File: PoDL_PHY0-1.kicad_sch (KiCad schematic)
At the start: 45 parts, among them Q1 DMG3414U, Q10 DMG3414U, Q11 DMG3414U, Q12 MMBT3904, Q2 MMBTA06, Q3 MMBT3904, Q4 DMG3414U, Q5 DMG3414U, Q6 MMBT3904, Q7 DMG3414U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

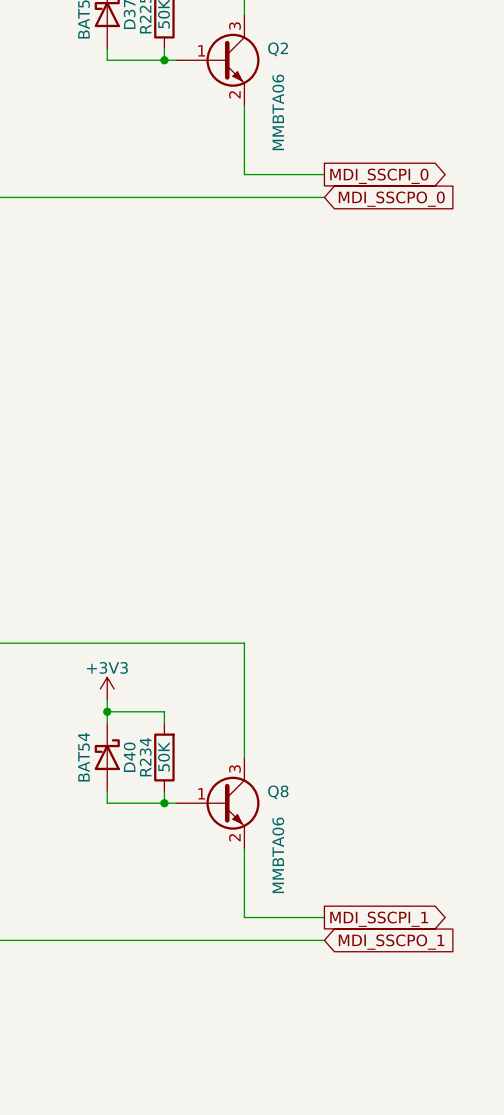
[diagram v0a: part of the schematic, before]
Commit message: Correcting SCCP spelling
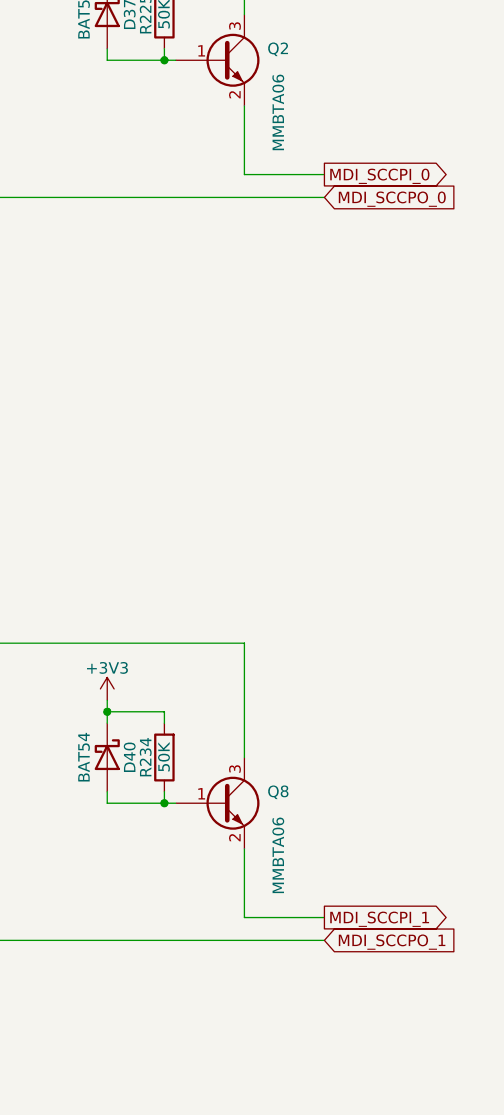
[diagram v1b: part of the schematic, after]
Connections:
- net MDI_SSCPI_0 renamed MDI_SCCPI_0
- net MDI_SSCPI_1 renamed MDI_SCCPI_1
- net MDI_SSCPO_0 renamed MDI_SCCPO_0
- net MDI_SSCPO_1 renamed MDI_SCCPO_1
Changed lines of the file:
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@@
     (effects (font (size 1.27 1.27)) (justify right bottom))
   )
-  (global_label "MDI_SSCPI_1" (shape output) (at 198.12 140.97 0) (fields_autoplaced)
+  (global_label "MDI_SCCPI_1" (shape output) (at 198.12 140.97 0) (fields_autoplaced)
     (effects (font (size 1.27 1.27)) (justify left))
     (property "Intersheet References" "${INTERSHEET_REFS}" (id 0) (at 212.5679 140.8906 0)
@@
     )
   )
-  (global_label "MDI_SSCPO_0" (shape input) (at 198.12 60.96 0) (fields_autoplaced)
+  (global_label "MDI_SCCPO_0" (shape input) (at 198.12 60.96 0) (fields_autoplaced)
     (effects (font (size 1.27 1.27)) (justify left))
     (property "Intersheet References" "${INTERSHEET_REFS}" (id 0) (at 213.2936 61.0394 0)
@@
     )
   )
-  (global_label "MDI_SSCPO_1" (shape input) (at 198.12 143.51 0) (fields_autoplaced)
+  (global_label "MDI_SCCPO_1" (shape input) (at 198.12 143.51 0) (fields_autoplaced)
     (effects (font (size 1.27 1.27)) (justify left))
     (property "Intersheet References" "${INTERSHEET_REFS}" (id 0) (at 213.2936 143.4306 0)
@@
     )
   )
-  (global_label "MDI_SSCPI_0" (shape output) (at 198.12 58.42 0) (fields_autoplaced)
+  (global_label "MDI_SCCPI_0" (shape output) (at 198.12 58.42 0) (fields_autoplaced)
     (effects (font (size 1.27 1.27)) (justify left))
     (property "Intersheet References" "${INTERSHEET_REFS}" (id 0) (at 212.5679 58.4994 0)
